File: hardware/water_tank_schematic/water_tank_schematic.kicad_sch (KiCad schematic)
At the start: 1 part

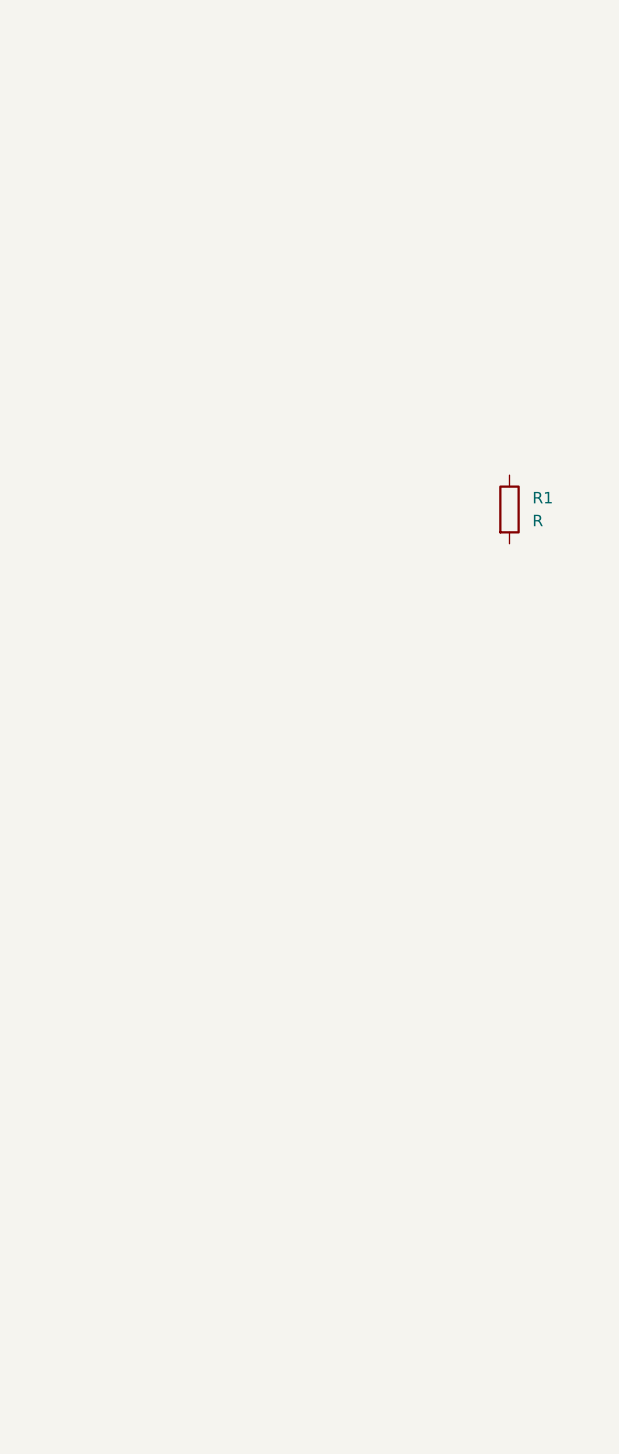
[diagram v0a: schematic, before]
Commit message: Build basic schematic
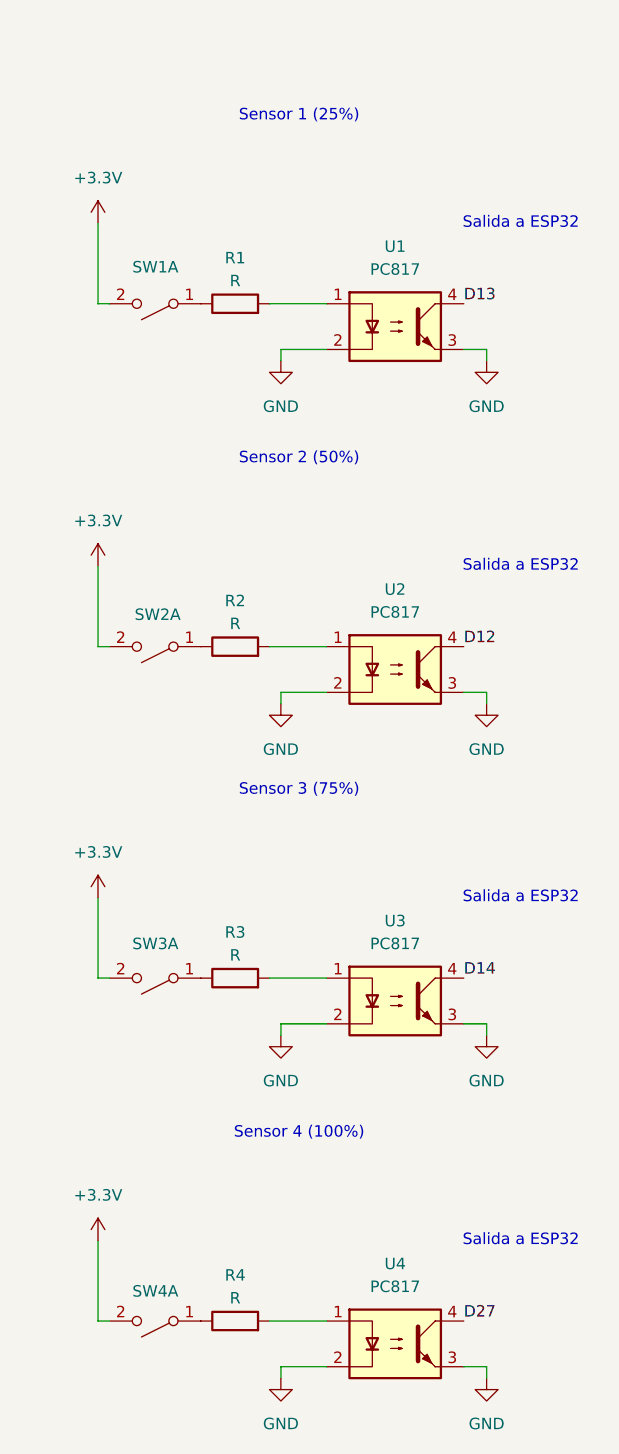
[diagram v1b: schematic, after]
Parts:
- added R2, R3, R4: R, symbol Device:R
- added SW1, SW2, SW3, SW4: (no value), symbol Switch:SW_DPST_x2
- added U1, U2, U3, U4: PC817, Package_DIP:DIP-4_W7.62mm, symbol Isolator:PC817
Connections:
- net at R1.1: now also SW1.1 (A)
- net at R1.2: now also U1.1
- new net: R2.2, U2.1
- new net: R4.1, SW4.1 (A)
- new net: R2.1, SW2.1 (A)
- new net: R3.2, U3.1
- new net: R4.2, U4.1
- new net: R3.1, SW3.1 (A)
- new net +3.3V: SW1.2 (B), SW2.2 (B), SW3.2 (B), SW4.2 (B)
- new net D12: U2.4
- new net D13: U1.4
- new net D14: U3.4
- new net D27: U4.4
- new net GND: U1.2, U1.3, U2.2, U2.3, U3.2, U3.3, U4.2, U4.3
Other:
- note added: "Salida a ESP32"
- note added: "Sensor 1 (25%)"
- note added: "Sensor 2 (50%)"
- note added: "Sensor 3 (75%)"
- note added: "Sensor 4 (100%)"
- moved on the sheet: R1

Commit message: Install mosquitto on rasberrypi
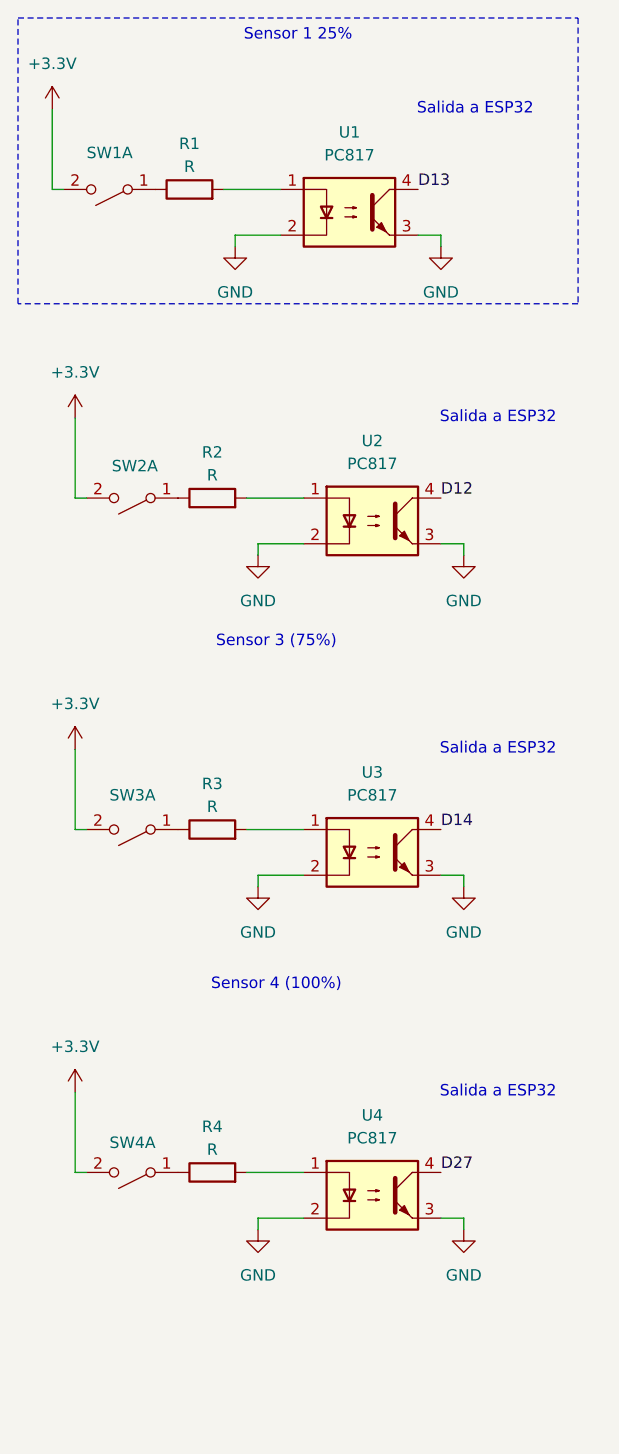
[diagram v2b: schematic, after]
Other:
- note removed: "Sensor 1 (25%)"
- note removed: "Sensor 2 (50%)"
- moved on the sheet: R1, R2, R3, R4, SW1A, SW2A, SW3A, SW4A, U1, U2, U3, U4
